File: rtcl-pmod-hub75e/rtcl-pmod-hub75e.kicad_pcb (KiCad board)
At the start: 4 copper layers, 20 x 56 mm, 24 parts, among them J1 PMOD, J2 HIF3FC-16PA-2.54DSA(71), J3 Conn_01x02, U1 74LVC273, U2 74LVC273, U3 74LVC273, U4 74LVC273, U5 LM809M3-2.93, U6 74LVC2G86

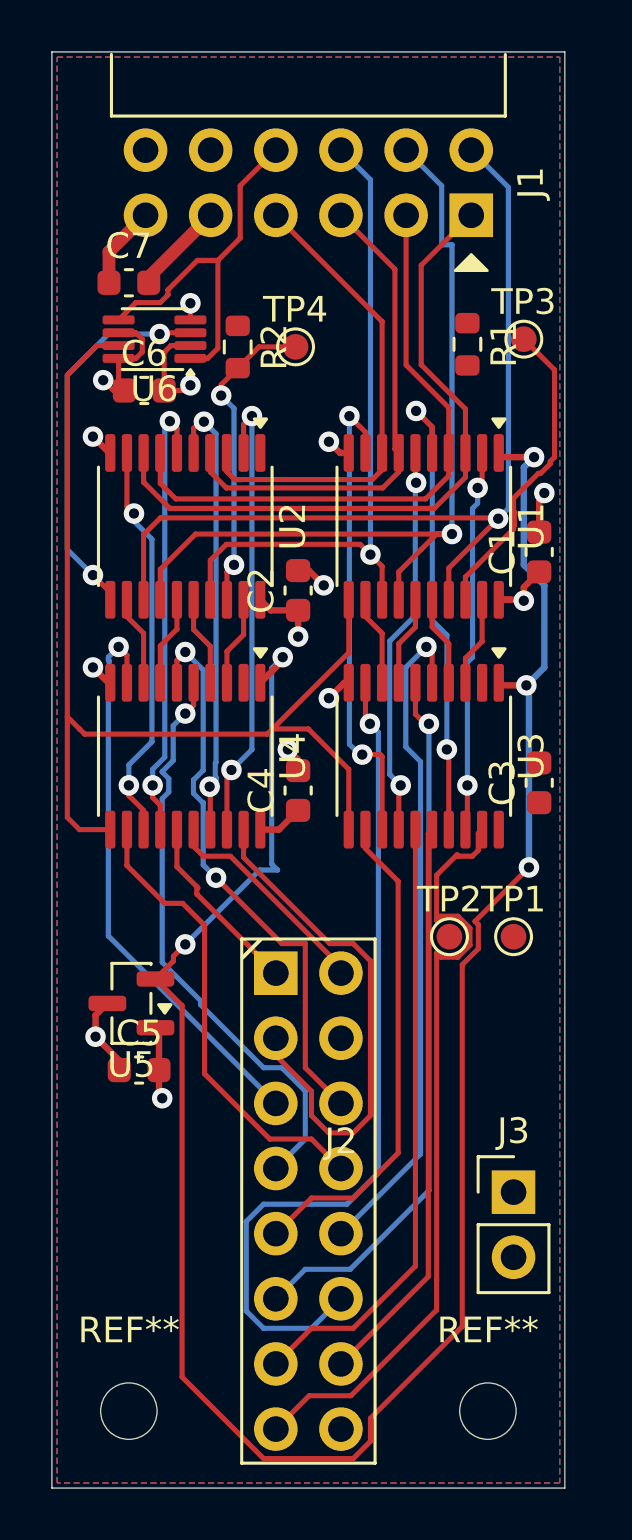
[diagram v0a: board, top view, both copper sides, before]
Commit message: Update selection filter settings in rtcl-pmod-hub75e.kicad_prl to enable footprints and vias
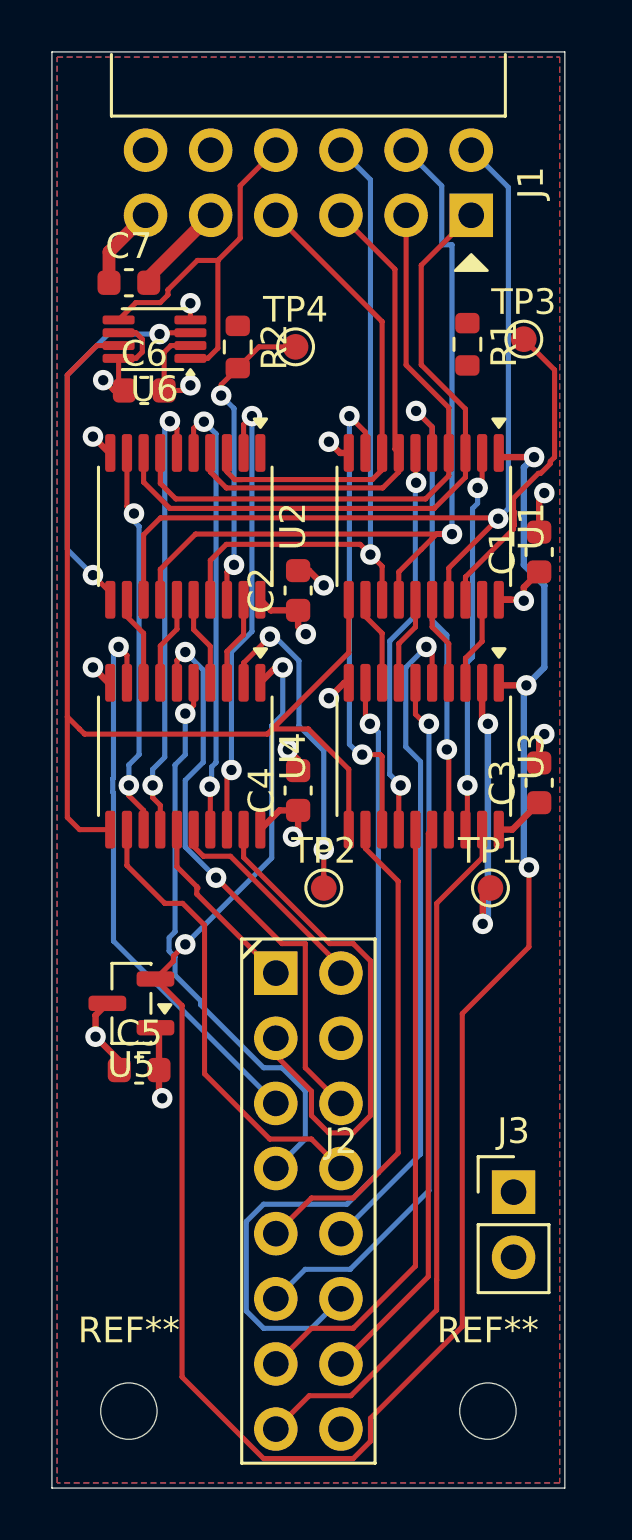
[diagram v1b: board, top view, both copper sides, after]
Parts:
- moved TP2 5.26 mm to (110.6, 82.6)
- moved TP1 2.10 mm to (117.1, 82.6)
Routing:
- net Net-(U4-Q0): track 0.00 -> 13.4 mm, vias 0 -> 2
- net Net-(U3-Q0): track 0.00 -> 11.1 mm, vias 0 -> 2
- net +3.3V: track 18.6 -> 21.7 mm, vias 4 -> 5
- net /HUB75_OE: track 30.6 -> 27.7 mm
- net /RESET: track 86.2 -> 84.6 mm
- net GND: track 18.5 -> 19.8 mm, vias 10 -> 11

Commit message: Update PCB and schematic files for rtcl-pmod-hub75e
- Changed active layer from 2 to 5 in the PCB layout.
- Modified visibility settings for text, tracks, and vias in the PCB layout.
- Updated visible layers in the PCB layout.
- Changed footprint references from "TestPoint" to "rtcl-pmod-hub75e" in the schematic.
- Updated UUIDs for various elements in the PH_02x08_2.54mm footprint.
- Added new footprint for TestPoint_Pad_D1.0mm.
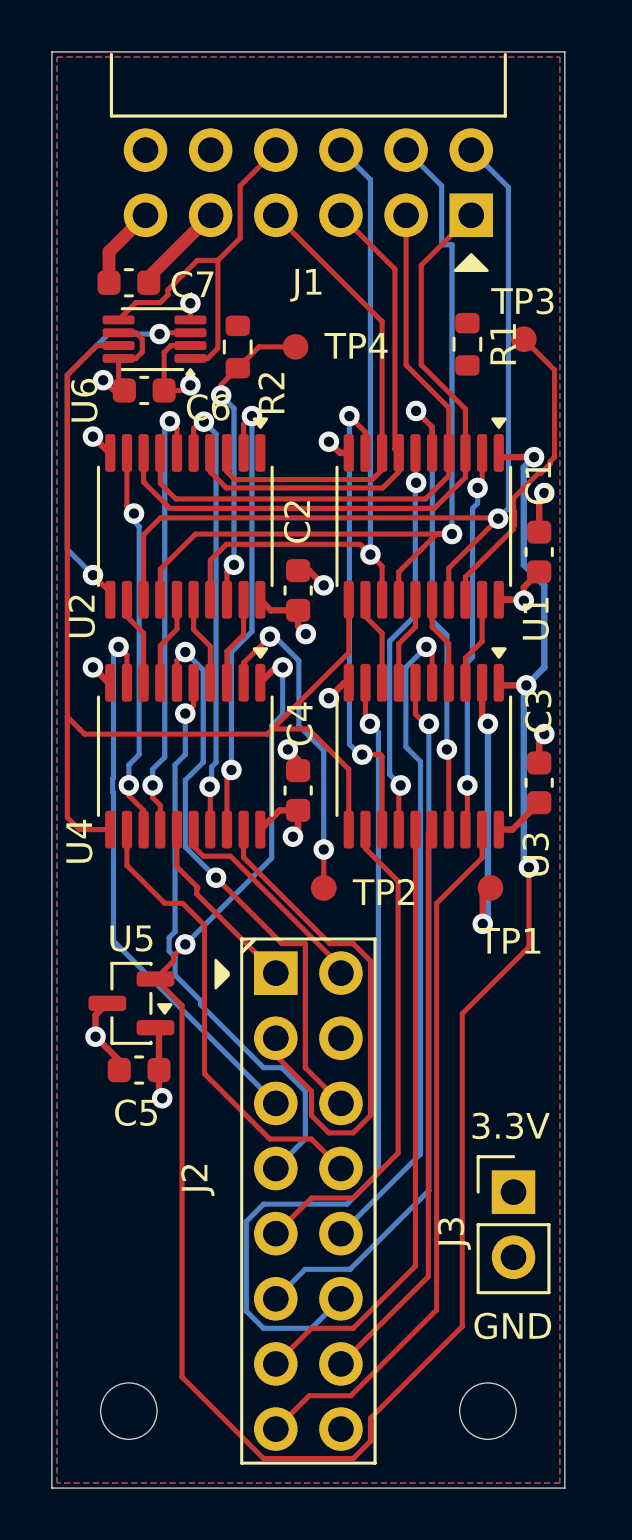
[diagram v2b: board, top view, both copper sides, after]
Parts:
- TP1, TP2, TP3, TP4: footprint TestPoint:TestPoint_Pad_D1.0mm -> rtcl-pmod-hub75e:TestPoint_Pad_D1.0mm
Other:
- board text added: "3.3V"
- board text added: "GND"
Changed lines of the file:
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@@
 		)
 	)
-	(footprint "TestPoint:TestPoint_Pad_D1.0mm"
+	(footprint "rtcl-pmod-hub75e:TestPoint_Pad_D1.0mm"
 		(layer "F.Cu")
 		(at 117.1 82.6)
@@
 		(tags "test point SMD pad")
 		(property "Reference" "TP1"
-			(at 0 -1.448 0)
+			(at 0.8 2.1 0)
 			(layer "F.SilkS")
 			(effects
@@
 		(fp_circle
 			(center 0 0)
-			(end 0 0.7)
-			(stroke
-				(width 0.12)
-				(type solid)
-			)
-			(fill no)
-			(layer "F.SilkS")
-		)
-		(fp_circle
-			(center 0 0)
 			(end 1 0)
 			(stroke
@@
 		(tags "TSSOP SO")
 		(property "Reference" "U3"
-			(at 0 -4.2 90)
+			(at 3.8375 -4.4 90)
 			(layer "F.SilkS")
 			(effects
@@
 		)
 	)
-	(footprint "TestPoint:TestPoint_Pad_D1.0mm"
+	(footprint "rtcl-pmod-hub75e:TestPoint_Pad_D1.0mm"
 		(layer "F.Cu")
 		(at 110.6 82.6)
@@
 		(tags "test point SMD pad")
 		(property "Reference" "TP2"
-			(at 0 -1.448 0)
+			(at 2.4 0.2 0)
 			(layer "F.SilkS")
 			(effects
@@
 		(fp_circle
 			(center 0 0)
-			(end 0 0.7)
-			(stroke
-				(width 0.12)
-				(type solid)
-			)
-			(fill no)
-			(layer "F.SilkS")
-		)
-		(fp_circle
-			(center 0 0)
 			(end 1 0)
 			(stroke
@@
 			(at 0 -3.15 0)
 			(layer "F.SilkS")
+			(hide yes)
 			(effects
 				(font
@@
 		(tags "SOT TO_SOT_SMD")
 		(property "Reference" "U5"
-			(at 0 -2.4 0)
+			(at 0 2.5 0)
 			(layer "F.SilkS")
 			(effects
@@
 		(tags "capacitor")
 		(property "Reference" "C2"
-			(at 0 -1.43 90)
+			(at 2.7 0 90)
 			(layer "F.SilkS")
 			(effects
@@
 		(tags "capacitor")
 		(property "Reference" "C1"
-			(at 0 -1.43 90)
+			(at 2.7 0 90)
 			(layer "F.SilkS")
 			(effects
@@
 		)
 	)
-	(footprint "TestPoint:TestPoint_Pad_D1.0mm"
+	(footprint "rtcl-pmod-hub75e:TestPoint_Pad_D1.0mm"
 		(layer "F.Cu")
 		(at 118.4 61.2)
@@
 		(fp_circle
 			(center 0 0)
-			(end 0 0.7)
-			(stroke
-				(width 0.12)
-				(type solid)
-			)
-			(fill no)
-			(layer "F.SilkS")
-		)
-		(fp_circle
-			(center 0 0)
 			(end 1 0)
 			(stroke
@@
 		(embedded_fonts no)
 	)
-	(footprint "TestPoint:TestPoint_Pad_D1.0mm"
+	(footprint "rtcl-pmod-hub75e:TestPoint_Pad_D1.0mm"
 		(layer "F.Cu")
 		(at 109.5 61.5)
@@
 		(tags "test point SMD pad")
 		(property "Reference" "TP4"
-			(at 0 -1.448 0)
+			(at 2.4 0 0)
 			(layer "F.SilkS")
 			(effects
@@
 		(fp_circle
 			(center 0 0)
-			(end 0 0.7)
-			(stroke
-				(width 0.12)
-				(type solid)
-			)
-			(fill no)
-			(layer "F.SilkS")
-		)
-		(fp_circle
-			(center 0 0)
 			(end 1 0)
 			(stroke
@@
 		(tags "capacitor")
 		(property "Reference" "C6"
-			(at 0 -1.43 0)
+			(at 2.5 0.7 0)
 			(layer "F.SilkS")
 			(effects
@@
 		(tags "capacitor")
 		(property "Reference" "C3"
-			(at 0 -1.43 90)
+			(at 2.8 0 90)
 			(layer "F.SilkS")
 			(effects
@@
 		(tags "Through hole pin header THT 2x06 2.54mm double row")
 		(property "Reference" "J2"
-			(at 1.27 -2.33 0)
+			(at -4.4 -0.91 90)
 			(layer "F.SilkS")
 			(effects
@@
 		)
 		(fp_line
-			(start -1.87 -10.19)
-			(end -2.57 -9.49)
+			(start -2.1 -10.2)
+			(end -2.57 -9.73)
 			(stroke
 				(width 0.15)
@@
 			(layer "F.SilkS")
 		)
+		(fp_poly
+			(pts
+				(xy -3.612056 -9.4) (xy -3.612056 -8.3) (xy -3.112056 -8.8) (xy -3.112056 -8.9)
+			)
+			(stroke
+				(width 0.1)
+				(type solid)
+			)
+			(fill yes)
+			(layer "F.SilkS")
+		)
 		(fp_line
 			(start -3.07 -10.69)
@@
 		(tags "Through hole pin header THT 2x06 2.54mm double row")
 		(property "Reference" "J1"
-			(at 0 -8.68 90)
+			(at 3.9 0 180)
 			(layer "F.SilkS")
 			(effects
@@
 			(at 0 -3.15 0)
 			(layer "F.SilkS")
+			(hide yes)
 			(effects
 				(font
@@
 		(tags "capacitor")
 		(property "Reference" "C5"
-			(at 0 -1.43 0)
+			(at -0.1 1.7 0)
 			(layer "F.SilkS")
 			(effects
@@
 		(tags "capacitor")
 		(property "Reference" "C4"
-			(at 0 -1.43 90)
+			(at 2.6 0.1 90)
 			(layer "F.SilkS")
 			(effects
@@
 		(tags "VSSOP SO JEDEC-MO-187-CA Texas_DCU0008A")
 		(property "Reference" "U6"
-			(at 0 -1.95 0)
+			(at 2.7 -2.4 90)
 			(layer "F.SilkS")
 			(effects
@@
 		(tags "TSSOP SO")
 		(property "Reference" "U2"
-			(at 0 -4.2 90)
+			(at 3.5 4 90)
 			(layer "F.SilkS")
 			(effects
@@
 		(tags "TSSOP SO")
 		(property "Reference" "U1"
-			(at 0 -4.2 90)
+			(at 3.6 -4.4 90)
 			(layer "F.SilkS")
 			(effects
@@
 		(tags "Through hole pin header THT 1x02 2.54mm single row")
 		(property "Reference" "J3"
-			(at 0 -2.38 0)
+			(at -2.4 1.54 90)
 			(layer "F.SilkS")
 			(effects
@@
 		(tags "capacitor")
 		(property "Reference" "C7"
-			(at 0 -1.43 0)
+			(at 2.5 0.1 0)
 			(layer "F.SilkS")
 			(effects
@@
 		(tags "TSSOP SO")
 		(property "Reference" "U4"
-			(at 0 -4.2 90)
+			(at 3.3375 4.1 90)
 			(layer "F.SilkS")
 			(effects
@@
 		(tags "resistor")
 		(property "Reference" "R2"
-			(at 0 -1.43 90)
+			(at 1.795 -1.355 90)
 			(layer "F.SilkS")
 			(effects
@@
 		(layer "Edge.Cuts")
 	)
+	(gr_text "3.3V"
+		(at 116.3 92.5 0)
+		(layer "F.SilkS")
+		(effects
+			(font
+				(size 1 1)
+				(thickness 0.15)
+			)
+			(justify left bottom)
+		)
+	)
+	(gr_text "GND\n"
+		(at 116.4 100.3 0)
+		(layer "F.SilkS")
+		(effects
+			(font
+				(size 1 1)
+				(thickness 0.15)
+			)
+			(justify left bottom)
+		)
+	)
 	(segment

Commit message: Update active layer and selection filter settings in KiCad project files
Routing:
- net /RESET: track 84.6 -> 94.4 mm, vias 5 -> 6
- net Net-(U1-D7): track 12.2 -> 14.8 mm
- net +3.3V: track 21.7 -> 22.8 mm, vias 5 -> 6
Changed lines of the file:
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@@
 		(tags "resistor")
 		(property "Reference" "R1"
-			(at 0 -1.43 90)
+			(at 0.7 1.4 90)
 			(layer "F.SilkS")
 			(effects
@@
 	)
 	(segment
+		(start 108.3625 65.4)
+		(end 108.125 65.6375)
+		(width 0.2)
+		(layer "F.Cu")
+		(net "/RESET")
+	)
+	(segment
 		(start 116 99.7)
 		(end 116 87.5)
@@
 	)
 	(segment
+		(start 108.7 65.4)
+		(end 108.3625 65.4)
+		(width 0.2)
+		(layer "F.Cu")
+		(net "/RESET")
+	)
+	(segment
 		(start 118.6 84.9)
 		(end 118.6 81.8)
@@
 	)
 	(via
+		(at 108.7 65.4)
+		(size 0.8)
+		(drill 0.4)
+		(layers "F.Cu" "B.Cu")
+		(net "/RESET")
+	)
+	(via
 		(at 105.2 84.8)
 		(size 0.8)
@@
 	)
 	(segment
+		(start 108.265477 65.834523)
+		(end 108.7 65.4)
+		(width 0.2)
+		(layer "B.Cu")
+		(net "/RESET")
+	)
+	(segment
 		(start 118.4 74.8)
 		(end 118.5 74.7)
@@
 	)
 	(segment
+		(start 109 74)
+		(end 108.265477 73.265478)
+		(width 0.2)
+		(layer "B.Cu")
+		(net "/RESET")
+	)
+	(segment
+		(start 108.265477 73.265478)
+		(end 108.265477 65.834523)
+		(width 0.2)
+		(layer "B.Cu")
+		(net "/RESET")
+	)
+	(segment
 		(start 119.2 70.8)
 		(end 119.2 74)
@@
 	)
 	(segment
+		(start 119 80.2)
+		(end 119.1 80.3)
+		(width 0.25)
+		(layer "F.Cu")
+		(net "+3.3V")
+	)
+	(segment
 		(start 109.6 79.575)
 		(end 108.875 79.575)
@@
 	)
 	(segment
+		(start 119 79.275)
+		(end 119 80.2)
+		(width 0.25)
+		(layer "F.Cu")
+		(net "+3.3V")
+	)
+	(segment
 		(start 102.625 89.325)
 		(end 101.7 88.4)
@@
 	)
 	(via
+		(at 119.1 80.3)
+		(size 0.8)
+		(drill 0.4)
+		(layers "F.Cu" "B.Cu")
+		(net "+3.3V")
+	)
+	(via
 		(at 102 62.8)
 		(size 0.8)
@@
 	(segment
 		(start 107.475 73.825)
-		(end 108.5 72.8)
+		(end 107.475 74.6)
 		(width 0.2)
 		(layer "F.Cu")
@@
 	)
 	(segment
-		(start 107.475 74.6)
-		(end 107.475 73.825)
+		(start 108.895477 73.004523)
+		(end 108.295477 73.004523)
 		(width 0.2)
 		(layer "F.Cu")
@@
 		(net "Net-(U4-Q0)")
 	)
+	(segment
+		(start 108.295477 73.004523)
+		(end 107.475 73.825)
+		(width 0.2)
+		(layer "F.Cu")
+		(net "Net-(U4-Q0)")
+	)
 	(via
-		(at 108.5 72.8)
+		(at 108.895477 73.004523)
 		(size 0.8)
 		(drill 0.4)
@@
 	)
 	(segment
-		(start 109.63 73.739045)
-		(end 109.63 76.278448)
-		(width 0.2)
-		(layer "B.Cu")
-		(net "Net-(U4-Q0)")
-	)
-	(segment
-		(start 110.6 77.248448)
-		(end 110.6 81.1)
+		(start 109.63 76.278448)
+		(end 110.6 77.248448)
 		(width 0.2)
 		(layer "B.Cu")
@@
 	)
 	(segment
-		(start 109.63 76.278448)
-		(end 110.6 77.248448)
+		(start 109.63 73.739045)
+		(end 109.63 76.278448)
 		(width 0.2)
 		(layer "B.Cu")
@@
 	)
 	(segment
-		(start 108.5 72.8)
-		(end 108.690955 72.8)
+		(start 110.6 77.248448)
+		(end 110.6 81.1)
 		(width 0.2)
 		(layer "B.Cu")
@@
 	)
 	(segment
-		(start 108.690955 72.8)
+		(start 108.895477 73.004523)
 		(end 109.63 73.739045)
 		(width 0.2)
@@
 	)
 	(segment
+		(start 116.2 62.225)
+		(end 117.375 62.225)
+		(width 0.2)
+		(layer "F.Cu")
+		(net "Net-(U1-D7)")
+	)
+	(segment
 		(start 119.6 65.8)
 		(end 119.6 62.4)
@@
 		(width 0.2)
 		(layer "F.Cu")
+		(net "Net-(U1-D7)")
+	)
+	(segment
+		(start 117.375 62.225)
+		(end 118.4 61.2)
+		(width 0.2)
+		(layer "F.Cu")

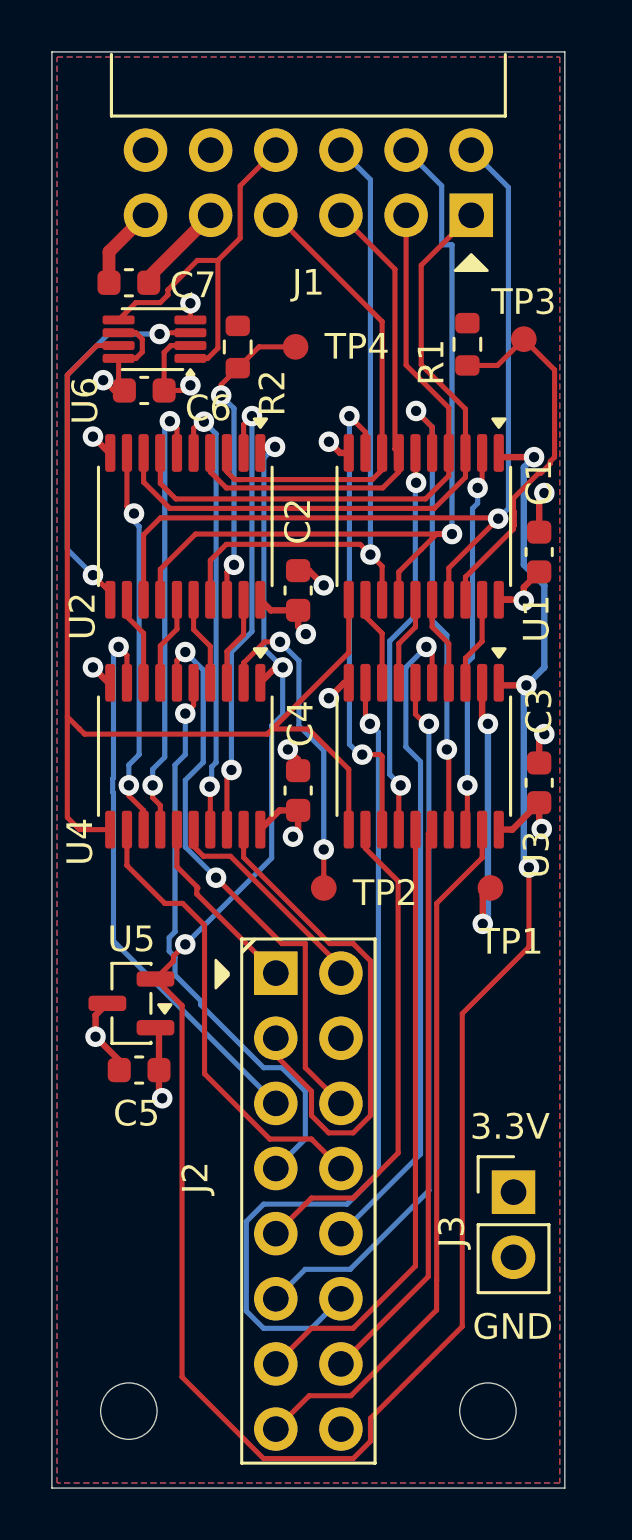
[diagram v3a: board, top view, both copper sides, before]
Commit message: Update active layer and selection filter settings in PCB layout
- Changed active layer from 0 to 4 for improved visibility.
- Modified selection filter to disable dimensions, footprints, graphics, keepouts, other items, pads, text, and zones for a cleaner interface.
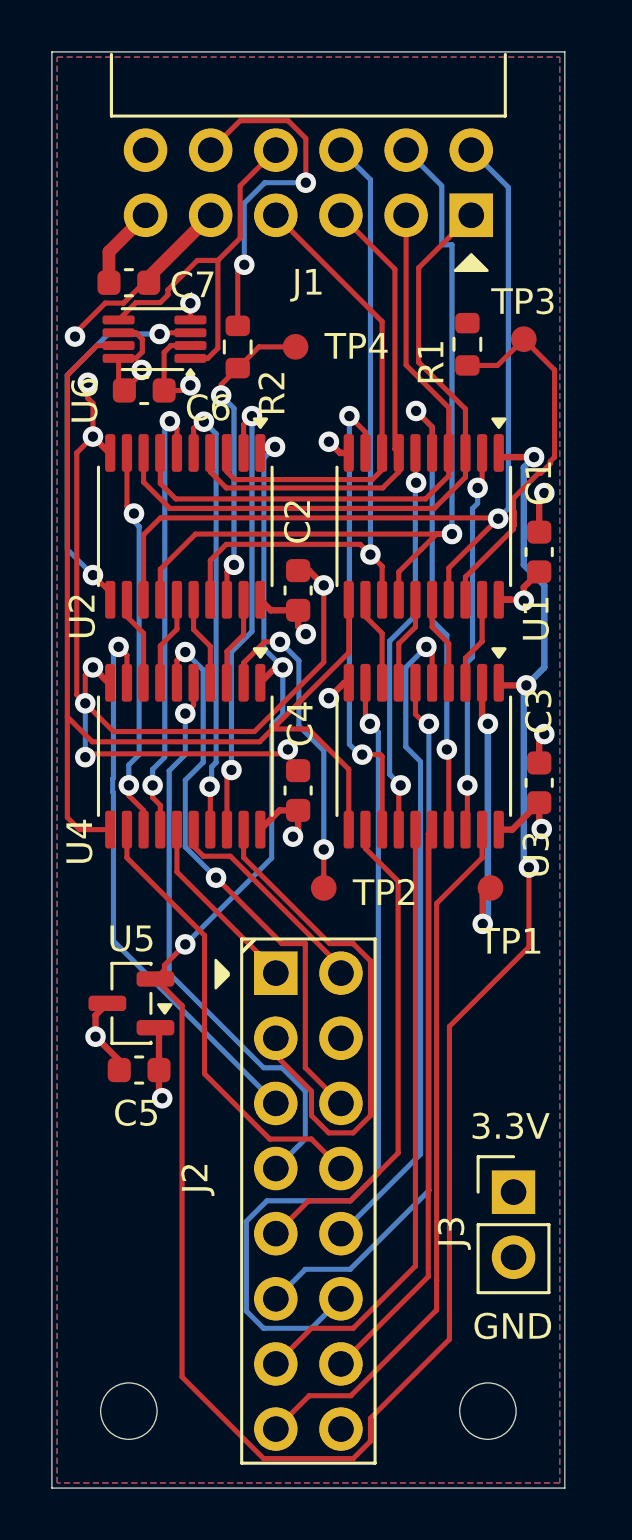
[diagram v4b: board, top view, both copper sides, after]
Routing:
- net GND: track 19.8 -> 76.9 mm, vias 11 -> 17
